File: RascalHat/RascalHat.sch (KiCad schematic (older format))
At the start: 7 parts, among them U1 Conn_01x04

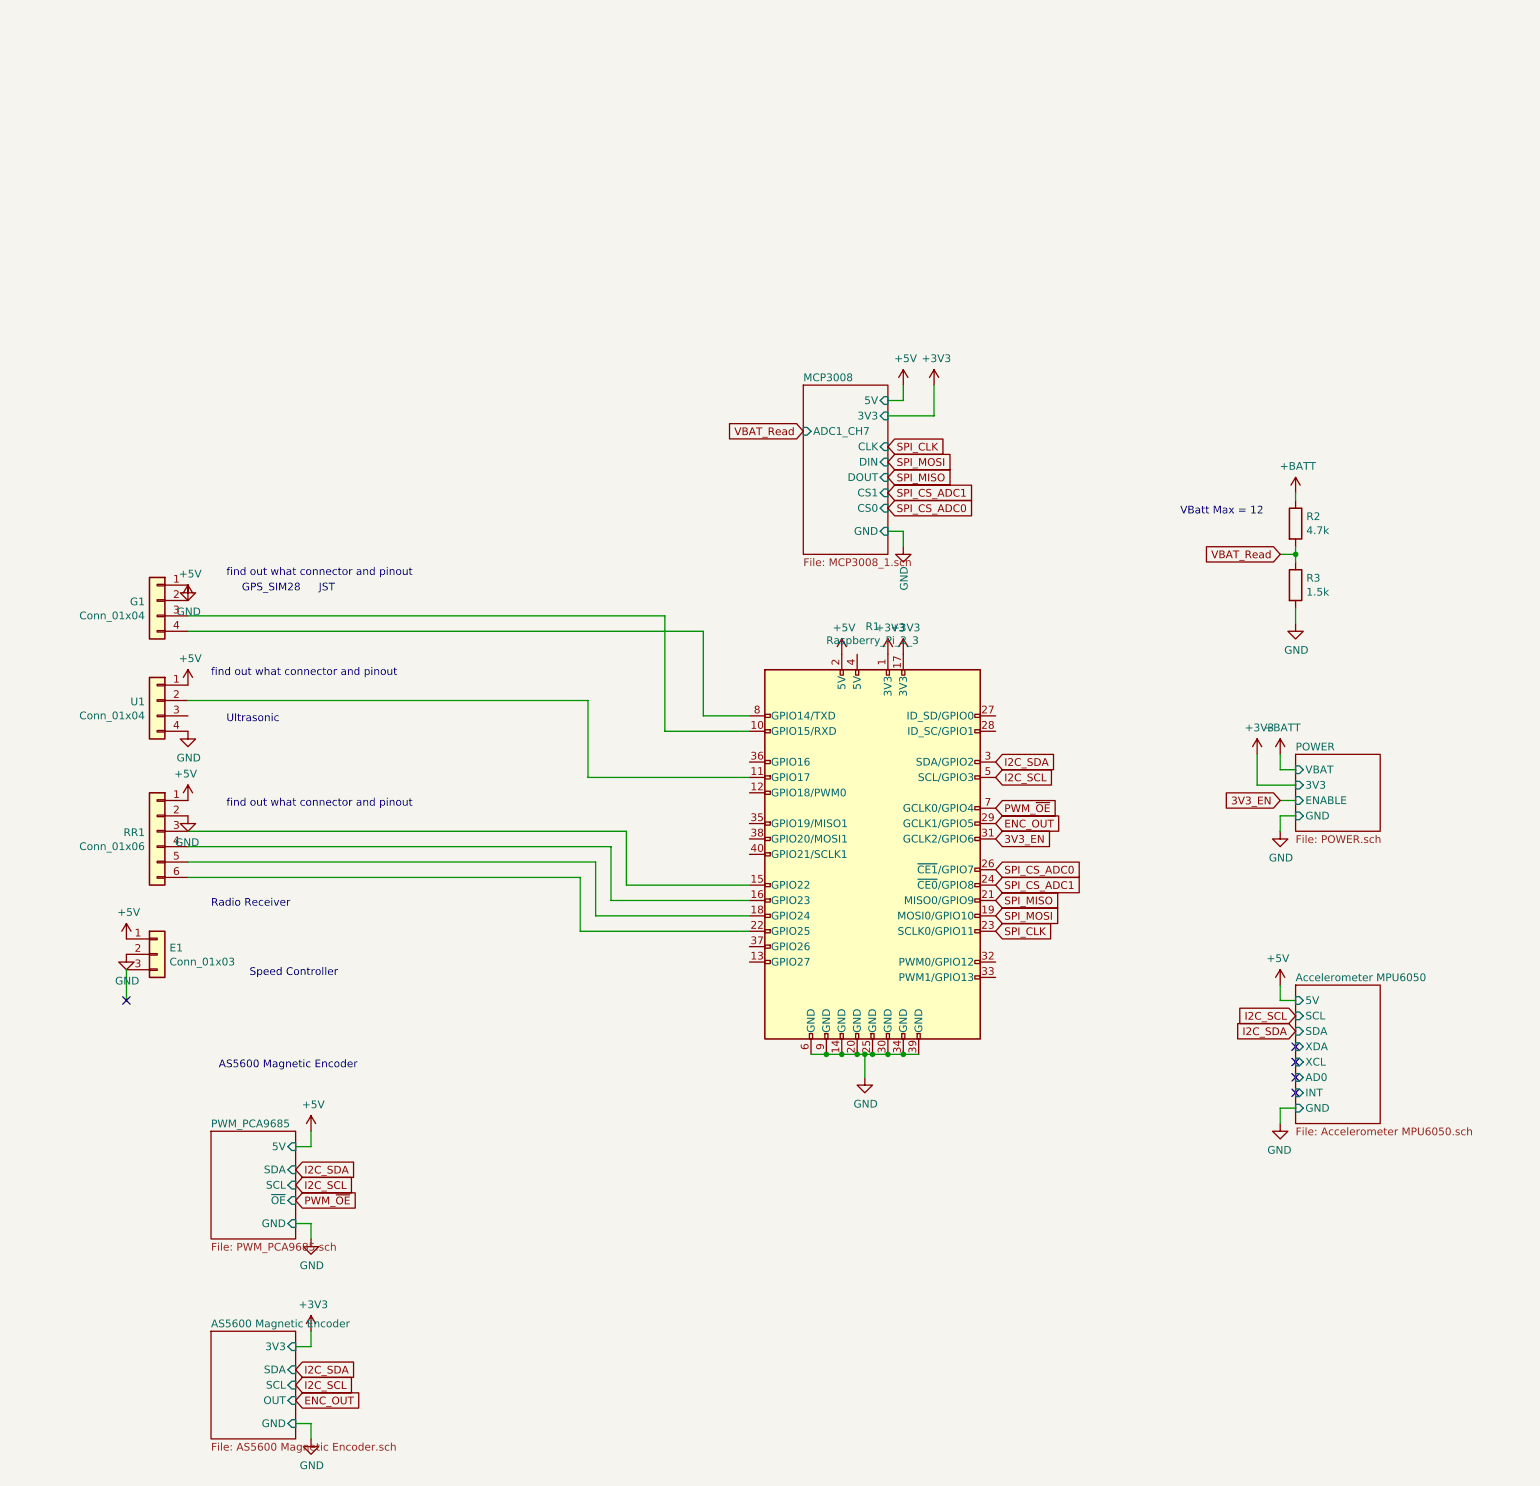
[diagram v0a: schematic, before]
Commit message: schematic done, symbol-footprint done, pcb started
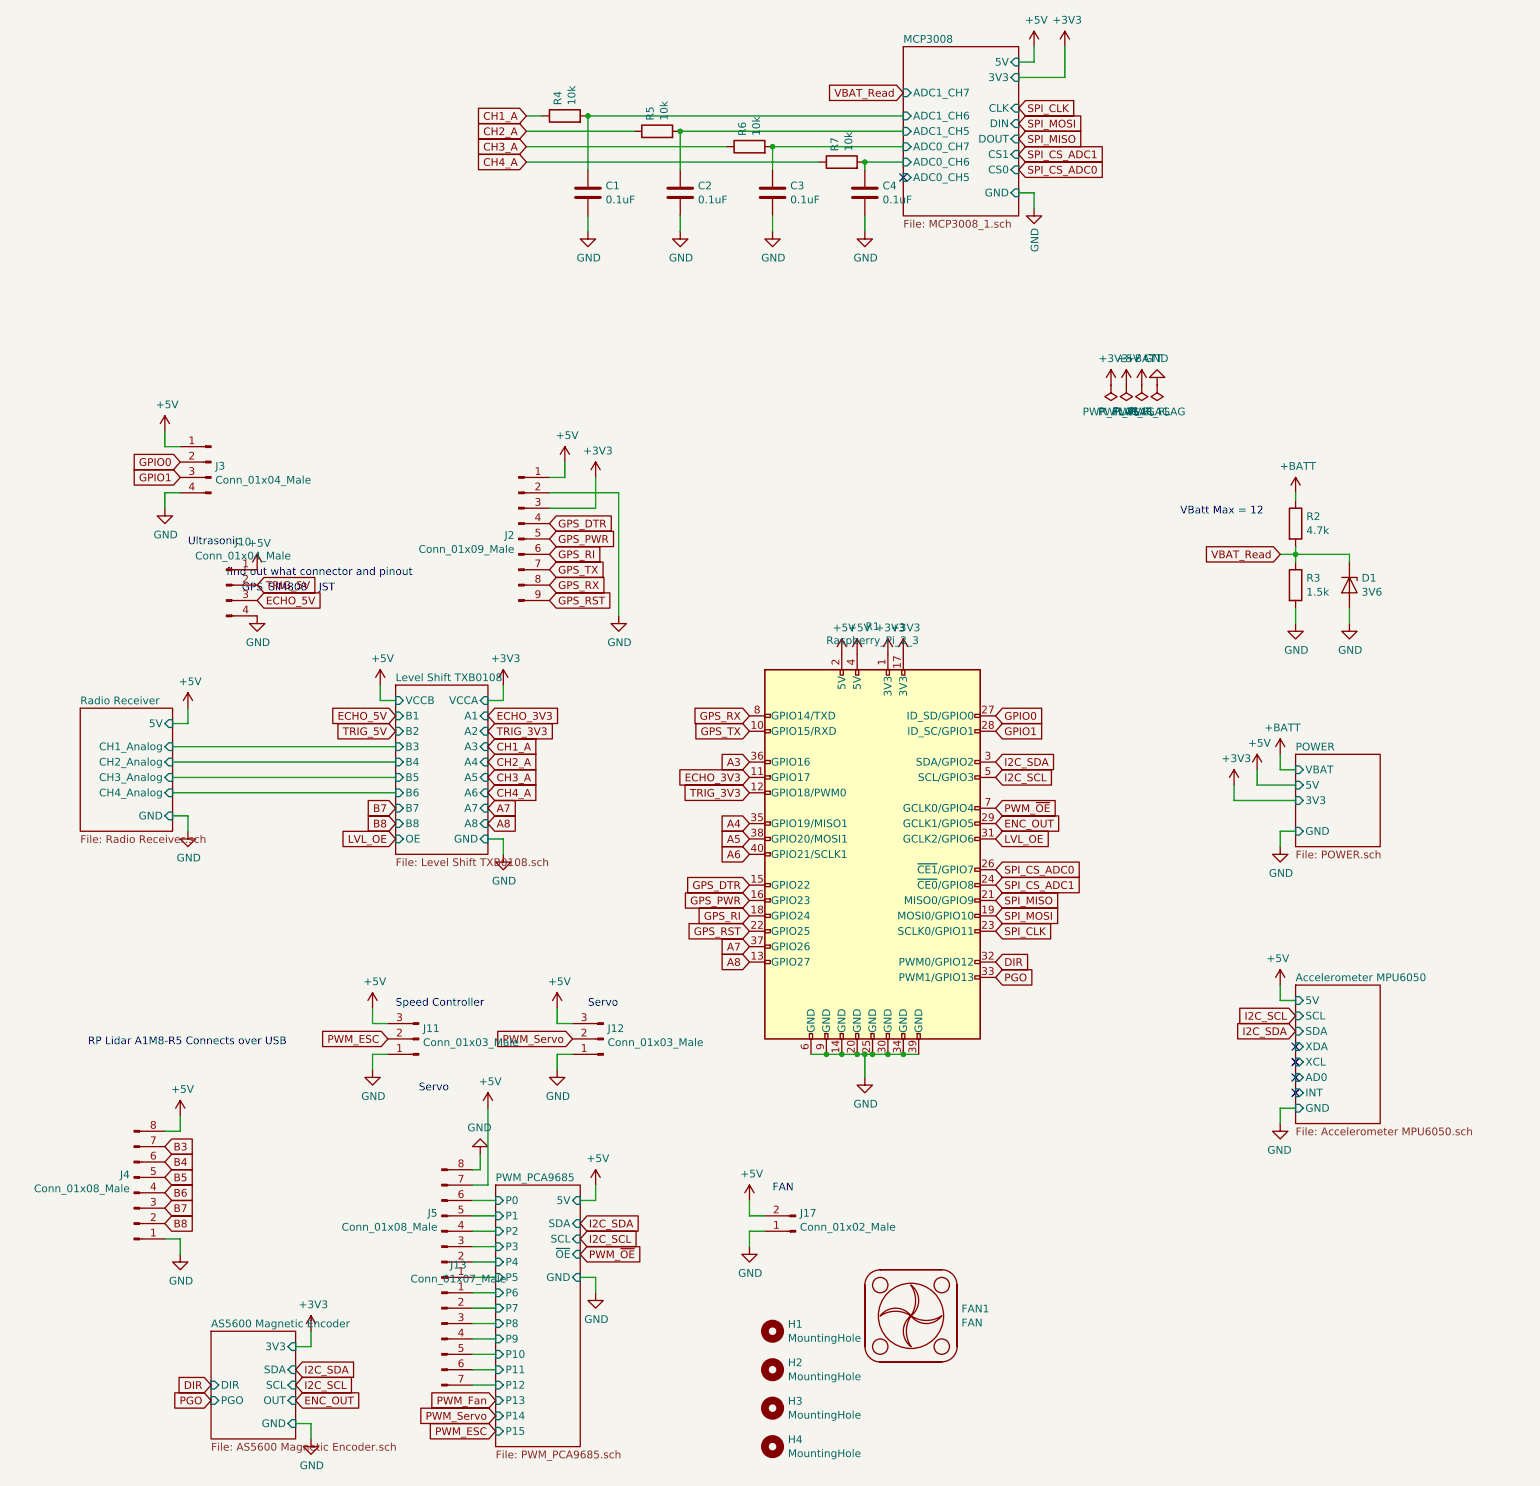
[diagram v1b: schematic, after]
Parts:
- removed E1: Conn_01x03, symbol Connector_Generic:Conn_01x03
- removed G1, U1: Conn_01x04, symbol Connector_Generic:Conn_01x04
- removed RR1: Conn_01x06, symbol Connector_Generic:Conn_01x06
- added C1, C2, C3, C4: 0.1uF, Capacitor_SMD:C_0805_2012Metric, symbol Device:C
- added D1: 3V6, Diode_SMD:D_SOD-323_HandSoldering, symbol Device:D_Zener
- added FAN1: FAN, RascalHat:25mm-FAN, symbol Rascal_KiCAD_LIB:FAN
- added H1, H2, H3, H4: MountingHole, MountingHole:MountingHole_3.2mm_M3, symbol Mechanical:MountingHole
- added J10, J3: Conn_01x04_Male, Connector_JST:JST_EH_B4B-EH-A_1x04_P2.50mm_Vertical, symbol Connector:Conn_01x04_Male
- added J11, J12: Conn_01x03_Male, Connector_JST:JST_EH_B3B-EH-A_1x03_P2.50mm_Vertical, symbol Connector:Conn_01x03_Male
- added J13: Conn_01x07_Male, Connector_JST:JST_EH_B7B-EH-A_1x07_P2.50mm_Vertical, symbol Connector:Conn_01x07_Male
- added J17: Conn_01x02_Male, Connector_JST:JST_EH_B2B-EH-A_1x02_P2.50mm_Vertical, symbol Connector:Conn_01x02_Male
- added J2: Conn_01x09_Male, Connector_JST:JST_EH_B9B-EH-A_1x09_P2.50mm_Vertical, symbol Connector:Conn_01x09_Male
- added J4, J5: Conn_01x08_Male, Connector_JST:JST_EH_B8B-EH-A_1x08_P2.50mm_Vertical, symbol Connector:Conn_01x08_Male
- added R4, R5, R6, R7: 10k, Resistor_SMD:R_0805_2012Metric, symbol Device:R
- R1: footprint (none) -> Connector_PinSocket_2.54mm:PinSocket_2x20_P2.54mm_Vertical
- R2, R3: footprint (none) -> Resistor_SMD:R_0805_2012Metric
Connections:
- net +3V3: now also J2.3 (Pin_3)
- net +5V: now also R1.4 (5V), J10.1 (Pin_1), J11.3 (Pin_3), J12.3 (Pin_3), J17.2 (Pin_2), J2.1 (Pin_1), J3.1 (Pin_1), J4.8 (Pin_8), J5.7 (Pin_7)
- net GND: now also C1.2, C2.2, C3.2, C4.2, D1.2 (A), J10.4 (Pin_4), J11.1 (Pin_1), J12.1 (Pin_1), J17.1 (Pin_1), J2.2 (Pin_2), J3.4 (Pin_4), J4.1 (Pin_1), J5.8 (Pin_8)
- net VBAT_Read: now also D1.1 (K)
- net GPS_TX: now reaches R1.10 (GPIO15/RXD)
- net GPS_TX: now also J2.7 (Pin_7)
- net ECHO_3V3: now reaches R1.11 (GPIO17)
- net TRIG_3V3: now reaches R1.12 (GPIO18/PWM0)
- net A8: now reaches R1.13 (GPIO27)
- net GPS_DTR: now reaches R1.15 (GPIO22)
- net GPS_DTR: now also J2.4 (Pin_4)
- net GPS_PWR: now reaches R1.16 (GPIO23)
- net GPS_PWR: now also J2.5 (Pin_5)
- net GPS_RI: now reaches R1.18 (GPIO24)
- net GPS_RI: now also J2.6 (Pin_6)
- net GPS_RST: now reaches R1.22 (GPIO25)
- net GPS_RST: now also J2.9 (Pin_9)
- net GPIO0: now reaches R1.27 (ID_SD/GPIO0)
- net GPIO0: now also J3.2 (Pin_2)
- net GPIO1: now reaches R1.28 (ID_SC/GPIO1)
- net GPIO1: now also J3.3 (Pin_3)
- net DIR: now reaches R1.32 (PWM0/GPIO12)
- net PGO: now reaches R1.33 (PWM1/GPIO13)
- net A4: now reaches R1.35 (GPIO19/MISO1)
- net A3: now reaches R1.36 (GPIO16)
- net A7: now reaches R1.37 (GPIO26)
- net A5: now reaches R1.38 (GPIO20/MOSI1)
- net A6: now reaches R1.40 (GPIO21/SCLK1)
- net GPS_RX: now reaches R1.8 (GPIO14/TXD)
- net GPS_RX: now also J2.8 (Pin_8)
- net 3V3_EN renamed LVL_OE
- new net B3: J4.7 (Pin_7)
- new net B4: J4.6 (Pin_6)
- new net B5: J4.5 (Pin_5)
- new net B6: J4.4 (Pin_4)
- new net B7: J4.3 (Pin_3)
- new net B8: J4.2 (Pin_2)
- new net CH1_A: R4.1
- new net CH2_A: R5.1
- new net CH3_A: R6.1
- new net CH4_A: R7.1
- new net ECHO_5V: J10.3 (Pin_3)
- new net MCP3008/ADC0_CH6: C4.1, R7.2
- new net MCP3008/ADC0_CH7: C3.1, R6.2
- new net MCP3008/ADC1_CH5: C2.1, R5.2
- new net MCP3008/ADC1_CH6: C1.1, R4.2
- new net PWM_ESC: J11.2 (Pin_2)
- new net PWM_PCA9685/P0: J5.6 (Pin_6)
- new net PWM_PCA9685/P1: J5.5 (Pin_5)
- new net PWM_PCA9685/P10: J13.5 (Pin_5)
- new net PWM_PCA9685/P11: J13.6 (Pin_6)
- new net PWM_PCA9685/P12: J13.7 (Pin_7)
- new net PWM_PCA9685/P2: J5.4 (Pin_4)
- new net PWM_PCA9685/P3: J5.3 (Pin_3)
- new net PWM_PCA9685/P4: J5.2 (Pin_2)
- new net PWM_PCA9685/P5: J5.1 (Pin_1)
- new net PWM_PCA9685/P6: J13.1 (Pin_1)
- new net PWM_PCA9685/P7: J13.2 (Pin_2)
- new net PWM_PCA9685/P8: J13.3 (Pin_3)
- new net PWM_PCA9685/P9: J13.4 (Pin_4)
- new net PWM_Servo: J12.2 (Pin_2)
- new net TRIG_5V: J10.2 (Pin_2)
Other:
- note added: "FAN"
- note added: "GPS_SIM808"
- note added: "RP Lidar A1M8-R5 Connects over USB"
- note added: "Servo"
- note removed: "AS5600 Magnetic Encoder"
- note removed: "GPS_SIM28"
- note removed: "Radio Receiver"
